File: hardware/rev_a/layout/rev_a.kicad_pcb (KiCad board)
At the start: 4 copper layers, 78 x 58 mm, 68 parts, among them J1 TSW-110-07-T-D, J2 TSW-110-07-T-D, U1 ADS1299-4PAGR, U2 TPS7A2033PDBVR

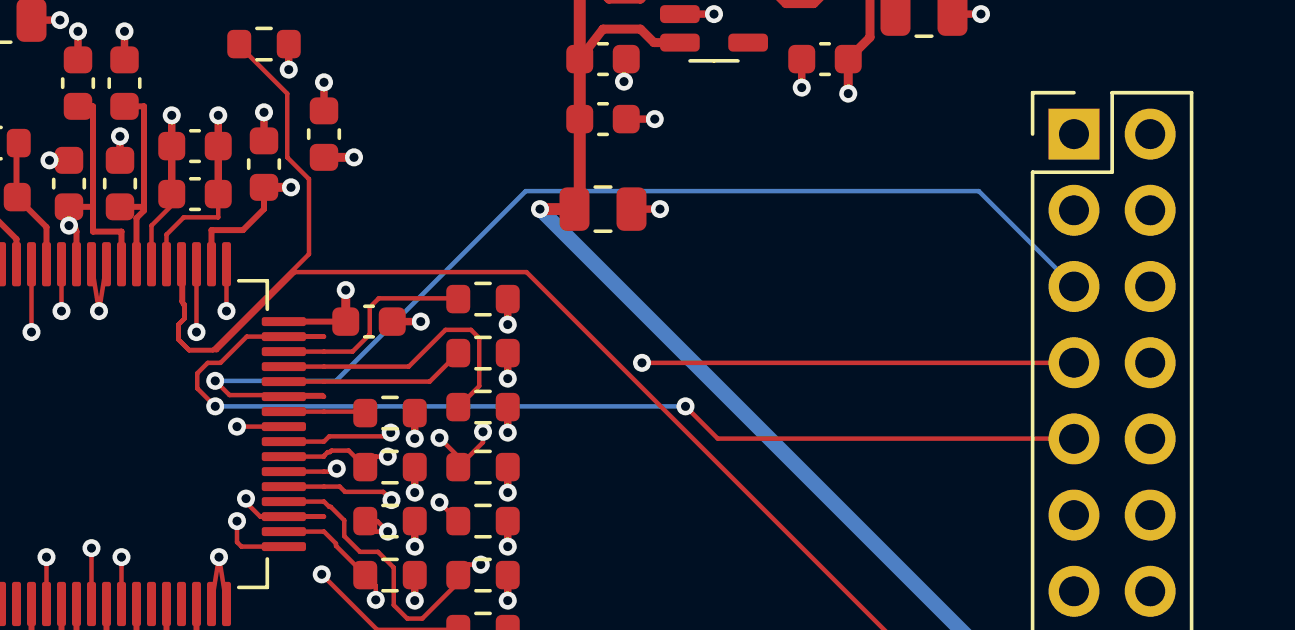
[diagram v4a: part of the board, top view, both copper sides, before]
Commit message: fix(hardware): reroute digital outputs over In1 with bounded local escapes
Preserve every footprint and all non-output copper. Move MISO and DRDY long spans from B to F, with short In2 escapes beside the ADC. Two original native red cases precede this repair. Connected wrong-layer and reference-window mutations are rejected; track reversal/subdivision are accepted. Existing output-cut locations now select new trunk segments. Four output-via fill openings are distinct after native refill. This is geometric layout verification, not measured noise or body-use qualification.
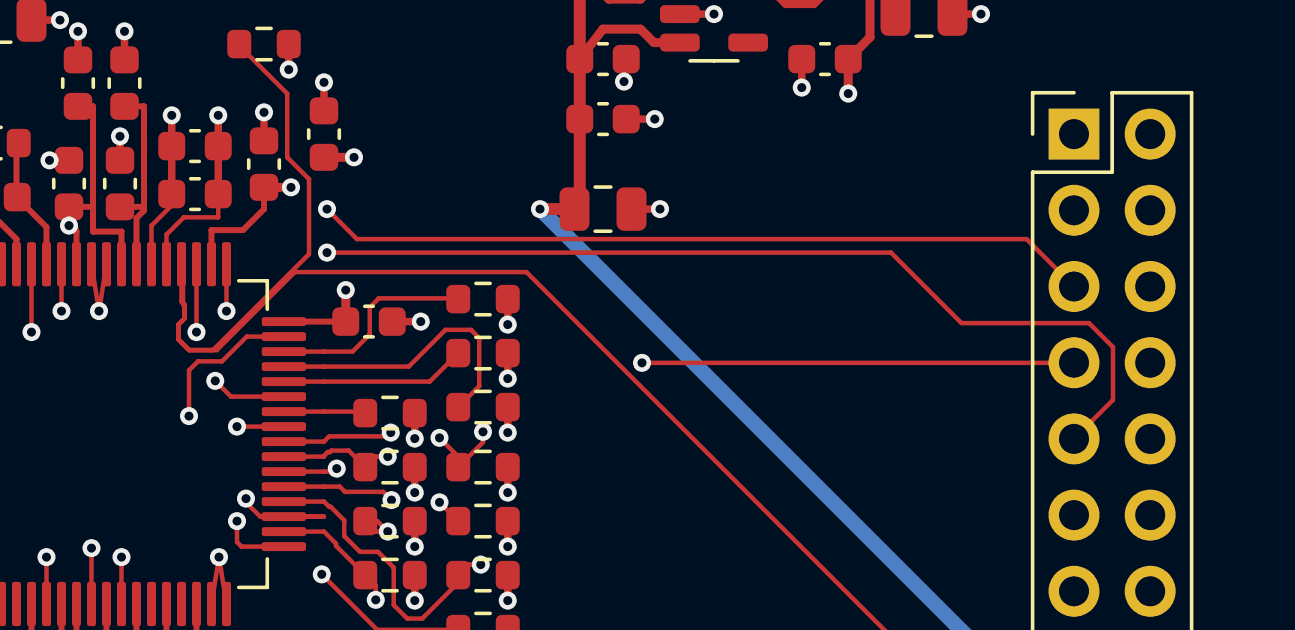
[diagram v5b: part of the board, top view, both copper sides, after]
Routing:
- net DRDY: track 36.5 -> 44.1 mm
- net MISO: track 37.7 -> 35.7 mm, vias 1 -> 2
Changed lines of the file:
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@@
 (segment (start 53.6625000 37.2500000) (end 55.0000000 37.2500000) (width 0.15) (layer "F.Cu") (net 35))
 (segment (start 53.6625000 36.2500000) (end 55.0000000 36.2500000) (width 0.15) (layer "F.Cu") (net 19))
-(segment (start 53.6625000 35.7500000) (end 55.0000000 35.7500000) (width 0.15) (layer "F.Cu") (net 31))
 (segment (start 53.6625000 35.2500000) (end 55.0000000 35.2500000) (width 0.15) (layer "F.Cu") (net 20))
 (segment (start 53.6625000 34.7500000) (end 55.0000000 34.7500000) (width 0.15) (layer "F.Cu") (net 21))
 (segment (start 53.6625000 34.2500000) (end 55.0000000 34.2500000) (width 0.15) (layer "F.Cu") (net 22))
-(segment (start 53.6625000 33.7500000) (end 55.0000000 33.7500000) (width 0.15) (layer "F.Cu") (net 16))
 (segment (start 50.2500000 31.3375000) (end 50.2500000 31.3250000) (width 0.15) (layer "F.Cu") (net 14))
 (segment (start 50.2500000 31.3250000) (end 50.2500000 32.5750000) (width 0.15) (layer "F.Cu") (net 14))
@@
 (segment (start 68.7250000 28.5000000) (end 78.5000000 28.5000000) (width 0.15) (layer "In2.Cu") (net 35))
 (segment (start 78.5000000 28.5000000) (end 80.0000000 27.0000000) (width 0.15) (layer "In2.Cu") (net 35))
-(segment (start 55.0000000 35.7500000) (end 54.9500000 35.7000000) (width 0.15) (layer "F.Cu") (net 31))
-(segment (start 54.9500000 35.7000000) (end 51.8500000 35.7000000) (width 0.15) (layer "F.Cu") (net 31))
-(segment (start 51.8500000 35.7000000) (end 51.3750000 35.2250000) (width 0.15) (layer "F.Cu") (net 31))
-(via (at 51.3750000 35.2250000) (size 0.6) (drill 0.3) (layers "F.Cu" "B.Cu") (net 31))
-(segment (start 51.3750000 35.2250000) (end 55.4000000 35.2250000) (width 0.15) (layer "B.Cu") (net 31))
-(segment (start 55.4000000 35.2250000) (end 61.7250000 28.9000000) (width 0.15) (layer "B.Cu") (net 31))
-(segment (start 61.7250000 28.9000000) (end 76.8250000 28.9000000) (width 0.15) (layer "B.Cu") (net 31))
-(segment (start 76.8250000 28.9000000) (end 80.0000000 32.0750000) (width 0.15) (layer "B.Cu") (net 31))
-(segment (start 80.0000000 32.0750000) (end 80.0000000 32.0800000) (width 0.15) (layer "B.Cu") (net 31))
-(segment (start 55.0000000 33.7500000) (end 52.4250000 33.7500000) (width 0.15) (layer "F.Cu") (net 16))
-(segment (start 52.4250000 33.7500000) (end 51.5500000 34.6250000) (width 0.15) (layer "F.Cu") (net 16))
-(segment (start 51.5500000 34.6250000) (end 51.1250000 34.6250000) (width 0.15) (layer "F.Cu") (net 16))
-(segment (start 51.1250000 34.6250000) (end 50.7750000 34.9750000) (width 0.15) (layer "F.Cu") (net 16))
-(segment (start 50.7750000 34.9750000) (end 50.7750000 35.4750000) (width 0.15) (layer "F.Cu") (net 16))
-(segment (start 50.7750000 35.4750000) (end 51.3750000 36.0750000) (width 0.15) (layer "F.Cu") (net 16))
-(via (at 51.3750000 36.0750000) (size 0.6) (drill 0.3) (layers "F.Cu" "B.Cu") (net 16))
-(segment (start 51.3750000 36.0750000) (end 67.0500000 36.0750000) (width 0.15) (layer "B.Cu") (net 16))
-(via (at 67.0500000 36.0750000) (size 0.6) (drill 0.3) (layers "F.Cu" "B.Cu") (net 16))
-(segment (start 67.0500000 36.0750000) (end 68.1250000 37.1500000) (width 0.15) (layer "F.Cu") (net 16))
-(segment (start 68.1250000 37.1500000) (end 80.0000000 37.1500000) (width 0.15) (layer "F.Cu") (net 16))
-(segment (start 80.0000000 37.1500000) (end 80.0000000 37.1600000) (width 0.15) (layer "F.Cu") (net 16))
 (segment (start 17.5400000 39.6200000) (end 17.5500000 39.6000000) (width 0.2) (layer "B.Cu") (net 11))
 (segment (start 17.5500000 39.6000000) (end 20.8000000 39.6000000) (width 0.2) (layer "B.Cu") (net 11))
@@
 (segment (start 46.8 24.525) (end 46.8 23.575) (width 0.25) (layer "F.Cu") (net 18))
 (via (at 46.8 23.575) (size 0.6) (drill 0.3) (layers "F.Cu" "B.Cu") (net 18))
+(segment (start 53.6625 35.75) (end 51.9 35.75) (width 0.15) (layer "F.Cu") (net 31))
+(segment (start 51.9 35.75) (end 51.375 35.225) (width 0.15) (layer "F.Cu") (net 31))
+(segment (start 55.1 29.5) (end 56.1 30.5) (width 0.15) (layer "F.Cu") (net 31))
+(segment (start 56.1 30.5) (end 78.42 30.5) (width 0.15) (layer "F.Cu") (net 31))
+(segment (start 78.42 30.5) (end 80 32.08) (width 0.15) (layer "F.Cu") (net 31))
+(segment (start 51.375 35.225) (end 53 33.6) (width 0.15) (layer "In2.Cu") (net 31))
+(segment (start 53 33.6) (end 53 31.6) (width 0.15) (layer "In2.Cu") (net 31))
+(segment (start 53 31.6) (end 55.1 29.5) (width 0.15) (layer "In2.Cu") (net 31))
+(via (at 51.3750000 35.2250000) (size 0.6) (drill 0.3) (layers "F.Cu" "B.Cu") (net 31))
+(via (at 55.1 29.5) (size 0.6) (drill 0.3) (layers "F.Cu" "B.Cu") (net 31))
+(segment (start 53.6625 33.75) (end 52.425 33.75) (width 0.15) (layer "F.Cu") (net 16))
+(segment (start 52.425 33.75) (end 51.6 34.575) (width 0.15) (layer "F.Cu") (net 16))
+(segment (start 51.6 34.575) (end 50.8 34.575) (width 0.15) (layer "F.Cu") (net 16))
+(segment (start 50.8 34.575) (end 50.5 34.875) (width 0.15) (layer "F.Cu") (net 16))
+(segment (start 50.5 34.875) (end 50.5 36.4) (width 0.15) (layer "F.Cu") (net 16))
+(segment (start 55.1 30.95) (end 73.9 30.95) (width 0.15) (layer "F.Cu") (net 16))
+(segment (start 73.9 30.95) (end 76.25 33.3) (width 0.15) (layer "F.Cu") (net 16))
+(segment (start 76.25 33.3) (end 80.5 33.3) (width 0.15) (layer "F.Cu") (net 16))
+(segment (start 80.5 33.3) (end 81.3 34.1) (width 0.15) (layer "F.Cu") (net 16))
+(segment (start 81.3 34.1) (end 81.3 35.86) (width 0.15) (layer "F.Cu") (net 16))
+(segment (start 81.3 35.86) (end 80 37.16) (width 0.15) (layer "F.Cu") (net 16))
+(segment (start 50.5 36.4) (end 51.4 36.4) (width 0.15) (layer "In2.Cu") (net 16))
+(segment (start 51.4 36.4) (end 53.8 34) (width 0.15) (layer "In2.Cu") (net 16))
+(segment (start 53.8 34) (end 53.8 32.275) (width 0.15) (layer "In2.Cu") (net 16))
+(segment (start 53.8 32.275) (end 55.1 30.95) (width 0.15) (layer "In2.Cu") (net 16))
+(via (at 50.5 36.4) (size 0.6) (drill 0.3) (layers "F.Cu" "B.Cu") (net 16))
+(via (at 55.1 30.95) (size 0.6) (drill 0.3) (layers "F.Cu" "B.Cu") (net 16))
 (zone
 		(net 18)

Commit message: fix(hardware): move CH1N outside the filtered input branch corridor
Preserve the failure-first native policy commit. Change only CH1N copper and fresh native-filled ground; retain all footprints, main filter paths and other nets. Add three harmful DRC-clean controls and three scoped benign controls. The route grows to 33.884 mm; this is not a noise or length-matching guarantee.
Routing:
- net CH1N_DUMMY: track 23.5 -> 33.9 mm
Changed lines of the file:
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@@
 (gr_text "DIGITAL / DEVKIT" (at 77 19) (layer "F.SilkS") (effects (font (size 0.85 0.85) (thickness 0.15))))
 (gr_text "NO BODY CONNECTION" (at 46 65) (layer "F.SilkS") (effects (font (size 1.0 1.0) (thickness 0.15))))
+(segment (start 17.54 32) (end 18.89 30.65) (width 0.2) (layer "F.Cu") (net 5))
+(segment (start 18.89 30.65) (end 30.9 30.65) (width 0.2) (layer "F.Cu") (net 5))
+(segment (start 30.9 30.65) (end 31 30.75) (width 0.2) (layer "F.Cu") (net 5))
+(segment (start 31 30.75) (end 33.6 30.75) (width 0.2) (layer "In2.Cu") (net 5))
+(segment (start 33.6 30.75) (end 34.9 32.05) (width 0.2) (layer "In2.Cu") (net 5))
+(segment (start 34.9 32.05) (end 34.9 43) (width 0.2) (layer "In2.Cu") (net 5))
+(segment (start 34.9 43) (end 31.7 43) (width 0.2) (layer "In2.Cu") (net 5))
+(segment (start 31.7000000 43.0000000) (end 31.7000000 44.2000000) (width 0.2) (layer "F.Cu") (net 5))
+(segment (start 31.7000000 44.2000000) (end 31.6750000 44.2250000) (width 0.2) (layer "F.Cu") (net 5))
+(via (at 31 30.75) (size 0.6) (drill 0.3) (layers "F.Cu" "B.Cu") (net 5))
+(via (at 31.7000000 43.0000000) (size 0.6) (drill 0.3) (layers "F.Cu" "B.Cu") (net 5))
 (segment (start 42.3375 40.75) (end 41.5 40.75) (width 0.15) (layer "F.Cu") (net 24))
 (segment (start 41.5 40.75) (end 36.475 45.775) (width 0.15) (layer "F.Cu") (net 24))
@@
 (segment (start 30.9500000 42.5000000) (end 31.7000000 41.7500000) (width 0.2) (layer "F.Cu") (net 8))
 (segment (start 31.7000000 41.7500000) (end 31.6750000 41.7750000) (width 0.2) (layer "F.Cu") (net 8))
-(segment (start 17.5400000 32.0000000) (end 17.5500000 32.0000000) (width 0.2) (layer "F.Cu") (net 5))
-(segment (start 17.5500000 32.0000000) (end 25.9000000 32.0000000) (width 0.2) (layer "F.Cu") (net 5))
-(segment (start 25.9000000 32.0000000) (end 25.9500000 31.9500000) (width 0.2) (layer "F.Cu") (net 5))
-(segment (start 25.9500000 31.9500000) (end 26.6000000 31.9500000) (width 0.2) (layer "F.Cu") (net 5))
-(segment (start 26.6000000 31.9500000) (end 27.0000000 32.3500000) (width 0.2) (layer "F.Cu") (net 5))
-(via (at 27.0000000 32.3500000) (size 0.6) (drill 0.3) (layers "F.Cu" "B.Cu") (net 5))
-(segment (start 27.0000000 32.3500000) (end 27.0000000 33.6500000) (width 0.2) (layer "In2.Cu") (net 5))
-(segment (start 27.0000000 33.6500000) (end 29.5000000 36.1500000) (width 0.2) (layer "In2.Cu") (net 5))
-(segment (start 29.5000000 36.1500000) (end 29.5000000 40.8000000) (width 0.2) (layer "In2.Cu") (net 5))
-(segment (start 29.5000000 40.8000000) (end 31.7000000 43.0000000) (width 0.2) (layer "In2.Cu") (net 5))
-(via (at 31.7000000 43.0000000) (size 0.6) (drill 0.3) (layers "F.Cu" "B.Cu") (net 5))
-(segment (start 31.7000000 43.0000000) (end 31.7000000 44.2000000) (width 0.2) (layer "F.Cu") (net 5))
-(segment (start 31.7000000 44.2000000) (end 31.6750000 44.2250000) (width 0.2) (layer "F.Cu") (net 5))
 (segment (start 15.0000000 32.0000000) (end 12.9000000 34.1000000) (width 0.2) (layer "F.Cu") (net 6))
 (segment (start 12.9000000 34.1000000) (end 12.9000000 46.8500000) (width 0.2) (layer "F.Cu") (net 6))

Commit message: fix(hardware): migrate both bench headers to the high-temperature HTSW selection
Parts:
- J1, J2: value TSW-110-07-T-D -> HTSW-110-07-T-D

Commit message: feat(hardware): author C3 native auxiliary and migrate loaded bus pulls
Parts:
- R12, R13, R15, R16, R17, R18, R19: value 10k -> 42.2k
